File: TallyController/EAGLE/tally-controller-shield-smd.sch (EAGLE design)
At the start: 40 parts, among them J2 Mega R3, U1 SN75174N, U2 SN75174N, U3 SN75174N

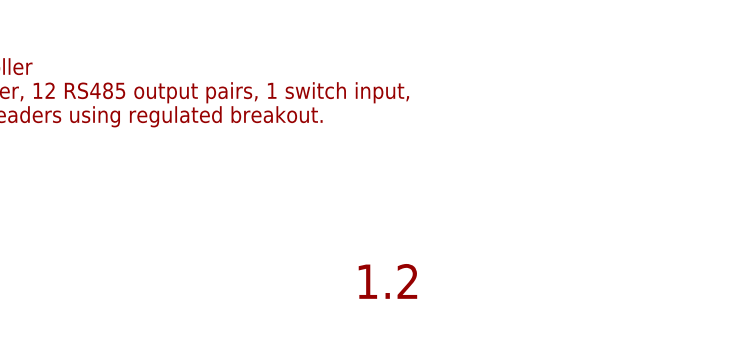
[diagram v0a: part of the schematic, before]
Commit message: Shift the RS485 drivers so they're aligned consistently
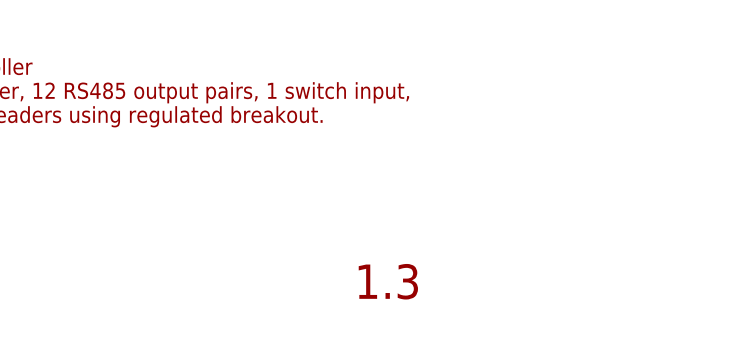
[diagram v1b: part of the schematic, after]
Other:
- note added: "1.3"
- note removed: "1.2"
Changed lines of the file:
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@@
 Includes I2C output header, NeoPixel header, 12 RS485 output pairs, 1 switch input,
 2 potentiometer inputs, XBee tranciever headers using regulated breakout.</text>
-<text x="71.12" y="-7.62" size="3.81" layer="94" align="top-left">1.2</text>
+<text x="71.12" y="-7.62" size="3.81" layer="94" align="top-left">1.3</text>
 </plain>
 <instances>
